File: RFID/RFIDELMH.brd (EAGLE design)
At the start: 21.6 x 39 mm, 3 parts, among them IC1 RFID_SENSOR, IC2 ARDUINO_PRO_MICRO

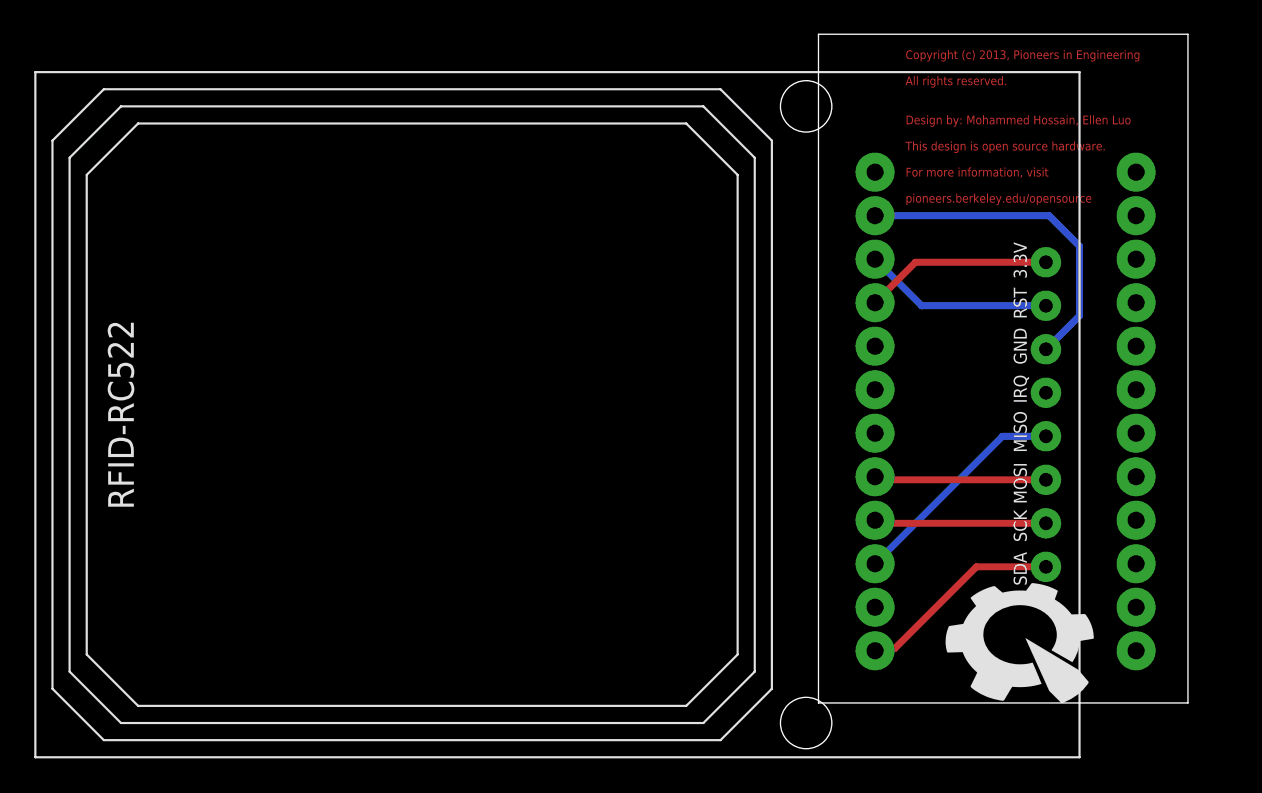
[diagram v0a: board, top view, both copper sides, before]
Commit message: Finish and flip RFID board
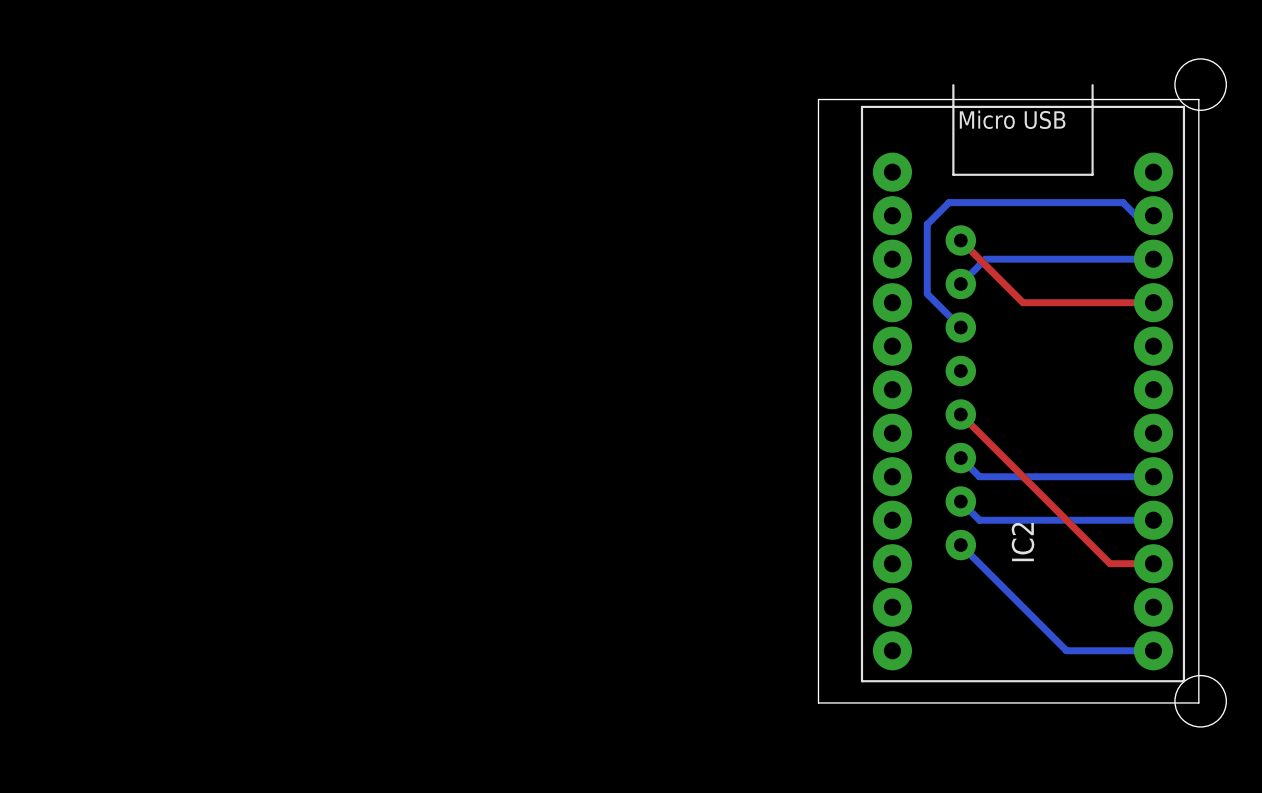
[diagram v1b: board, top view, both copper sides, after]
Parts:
- moved IC1 113.0 mm to (67.3, 38.1), flipped to the bottom
- moved IC2 17.8 mm to (2.54, 1.27), flipped to the top
- moved U$1 1.90 mm to (12.1, 5.71), flipped to the bottom
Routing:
- net SDA: track 12.0 -> 13.8 mm
- net MISO: track 13.1 -> 14.9 mm
- net VCC: track 11.0 -> 12.8 mm
- net SCK: track 10.1 -> 11.7 mm
- net MOSI: track 10.1 -> 11.7 mm
- net GND: track 19.5 -> 20.9 mm
- net RST: track 11.1 -> 11.8 mm
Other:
- board size 21.6 x 39 mm -> 22.2 x 35.2 mm
- board text added: "(c) Pioneers In Engineering Design by: Mohammed, Seiya, Averal, Ellen Catherine, Nick, Jillian, Lingfei, Ezra, Malcolm This design is open source hardware. For more information, visit: pioneers.berkeley.edu/opensource"
- board text removed: "Copyright (c) 2013, Pioneers in Engineering All rights reserved. Design by: Mohammed Hossain, Ellen Luo This design is open source hardware. For more information, visit pioneers.berkeley.edu/opensource"
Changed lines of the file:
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@@
 <layer number="27" name="tValues" color="7" fill="1" visible="yes" active="yes"/>
 <layer number="28" name="bValues" color="7" fill="1" visible="yes" active="yes"/>
-<layer number="29" name="tStop" color="7" fill="3" visible="no" active="yes"/>
-<layer number="30" name="bStop" color="7" fill="6" visible="no" active="yes"/>
-<layer number="31" name="tCream" color="7" fill="4" visible="no" active="yes"/>
-<layer number="32" name="bCream" color="7" fill="5" visible="no" active="yes"/>
-<layer number="33" name="tFinish" color="6" fill="3" visible="no" active="yes"/>
-<layer number="34" name="bFinish" color="6" fill="6" visible="no" active="yes"/>
-<layer number="35" name="tGlue" color="7" fill="4" visible="no" active="yes"/>
-<layer number="36" name="bGlue" color="7" fill="5" visible="no" active="yes"/>
-<layer number="37" name="tTest" color="7" fill="1" visible="no" active="yes"/>
-<layer number="38" name="bTest" color="7" fill="1" visible="no" active="yes"/>
+<layer number="29" name="tStop" color="7" fill="3" visible="yes" active="yes"/>
+<layer number="30" name="bStop" color="7" fill="6" visible="yes" active="yes"/>
+<layer number="31" name="tCream" color="7" fill="4" visible="yes" active="yes"/>
+<layer number="32" name="bCream" color="7" fill="5" visible="yes" active="yes"/>
+<layer number="33" name="tFinish" color="6" fill="3" visible="yes" active="yes"/>
+<layer number="34" name="bFinish" color="6" fill="6" visible="yes" active="yes"/>
+<layer number="35" name="tGlue" color="7" fill="4" visible="yes" active="yes"/>
+<layer number="36" name="bGlue" color="7" fill="5" visible="yes" active="yes"/>
+<layer number="37" name="tTest" color="7" fill="1" visible="yes" active="yes"/>
+<layer number="38" name="bTest" color="7" fill="1" visible="yes" active="yes"/>
 <layer number="39" name="tKeepout" color="4" fill="11" visible="yes" active="yes"/>
 <layer number="40" name="bKeepout" color="1" fill="11" visible="yes" active="yes"/>
@@
 <layer number="42" name="bRestrict" color="1" fill="10" visible="yes" active="yes"/>
 <layer number="43" name="vRestrict" color="2" fill="10" visible="yes" active="yes"/>
-<layer number="44" name="Drills" color="7" fill="1" visible="no" active="yes"/>
-<layer number="45" name="Holes" color="7" fill="1" visible="no" active="yes"/>
-<layer number="46" name="Milling" color="3" fill="1" visible="no" active="yes"/>
-<layer number="47" name="Measures" color="7" fill="1" visible="no" active="yes"/>
+<layer number="44" name="Drills" color="7" fill="1" visible="yes" active="yes"/>
+<layer number="45" name="Holes" color="7" fill="1" visible="yes" active="yes"/>
+<layer number="46" name="Milling" color="3" fill="1" visible="yes" active="yes"/>
+<layer number="47" name="Measures" color="7" fill="1" visible="yes" active="yes"/>
 <layer number="48" name="Document" color="7" fill="1" visible="yes" active="yes"/>
 <layer number="49" name="Reference" color="7" fill="1" visible="yes" active="yes"/>
@@
 <board>
 <plain>
-<wire x1="0" y1="0" x2="21.57" y2="0" width="0" layer="20"/>
-<wire x1="21.57" y1="0" x2="21.57" y2="39.04" width="0" layer="20"/>
-<wire x1="21.57" y1="39.04" x2="0" y2="39.04" width="0" layer="20"/>
-<wire x1="0" y1="39.04" x2="0" y2="0" width="0" layer="20"/>
-<text x="5.08" y="29.21" size="0.508" layer="1">Copyright (c) 2013, Pioneers in Engineering
-All rights reserved.
-Design by: Mohammed Hossain, Ellen Luo
+<wire x1="0" y1="0" x2="22.205" y2="0" width="0" layer="20"/>
+<wire x1="22.205" y1="0" x2="22.205" y2="35.23" width="0" layer="20"/>
+<wire x1="22.205" y1="35.23" x2="0" y2="35.23" width="0" layer="20"/>
+<wire x1="0" y1="35.23" x2="0" y2="0" width="0" layer="20"/>
+<text x="12.7" y="29.21" size="0.508" layer="23" font="vector" rot="R270">(c) Pioneers In Engineering
+Design by: Mohammed, Seiya, Averal, Ellen
+Catherine, Nick, Jillian, Lingfei, Ezra, Malcolm
 This design is open source hardware.
-For more information, visit
+For more information, visit:
 pioneers.berkeley.edu/opensource</text>
 </plain>
@@
 </autorouter>
 <elements>
-<element name="IC1" library="pie" package="RFID_SENSOR" value="RFID_SENSOR" x="-45.72" y="36.83" rot="R270"/>
-<element name="IC2" library="pie" package="ARDUINO_PRO_MICRO" value="ARDUINO_PRO_MICRO" x="20.32" y="1.27" rot="MR0"/>
-<element name="U$1" library="pie" package="PIE-LOGO-SMALL" value="" x="12.065" y="3.81"/>
+<element name="IC1" library="pie" package="RFID_SENSOR" value="RFID_SENSOR" x="67.31" y="38.1" rot="MR270"/>
+<element name="IC2" library="pie" package="ARDUINO_PRO_MICRO" value="ARDUINO_PRO_MICRO" x="2.54" y="1.27"/>
+<element name="U$1" library="pie" package="PIE-LOGO-SMALL" value="" x="12.065" y="5.715" rot="MR0"/>
 </elements>
 <signals>
@@
 <contactref element="IC2" pad="VCC"/>
 <contactref element="IC1" pad="3.3V"/>
-<wire x1="3.302" y1="23.368" x2="5.664" y2="25.73" width="0.4064" layer="1"/>
-<wire x1="5.664" y1="25.73" x2="13.28" y2="25.73" width="0.4064" layer="1"/>
+<wire x1="8.31" y1="27" x2="11.942" y2="23.368" width="0.4064" layer="1"/>
+<wire x1="11.942" y1="23.368" x2="19.558" y2="23.368" width="0.4064" layer="1"/>
 </signal>
 <signal name="RST">
 <contactref element="IC2" pad="RST"/>
 <contactref element="IC1" pad="RST"/>
-<wire x1="3.302" y1="25.908" x2="6.02" y2="23.19" width="0.4064" layer="16"/>
-<wire x1="6.02" y1="23.19" x2="13.28" y2="23.19" width="0.4064" layer="16"/>
+<wire x1="8.31" y1="24.46" x2="9.758" y2="25.908" width="0.4064" layer="16"/>
+<wire x1="9.758" y1="25.908" x2="19.558" y2="25.908" width="0.4064" layer="16"/>
 </signal>
 <signal name="GND">
 <contactref element="IC1" pad="GND"/>
 <contactref element="IC2" pad="GND@2"/>
-<wire x1="13.28" y1="20.65" x2="15.24" y2="22.61" width="0.4064" layer="16"/>
-<wire x1="15.24" y1="22.61" x2="15.24" y2="26.67" width="0.4064" layer="16"/>
-<wire x1="15.24" y1="26.67" x2="13.462" y2="28.448" width="0.4064" layer="16"/>
-<wire x1="13.462" y1="28.448" x2="3.302" y2="28.448" width="0.4064" layer="16"/>
+<wire x1="8.31" y1="21.92" x2="6.35" y2="23.88" width="0.4064" layer="16"/>
+<wire x1="6.35" y1="23.88" x2="6.35" y2="27.94" width="0.4064" layer="16"/>
+<wire x1="6.35" y1="27.94" x2="7.62" y2="29.21" width="0.4064" layer="16"/>
+<wire x1="7.62" y1="29.21" x2="17.78" y2="29.21" width="0.4064" layer="16"/>
+<wire x1="17.78" y1="29.21" x2="18.542" y2="28.448" width="0.4064" layer="16"/>
+<wire x1="18.542" y1="28.448" x2="19.558" y2="28.448" width="0.4064" layer="16"/>
 </signal>
 <signal name="SDA">
 <contactref element="IC2" pad="10"/>
 <contactref element="IC1" pad="SDA"/>
-<wire x1="13.28" y1="7.95" x2="9.22" y2="7.95" width="0.4064" layer="1"/>
-<wire x1="9.22" y1="7.95" x2="4.445" y2="3.175" width="0.4064" layer="1"/>
-<wire x1="4.445" y1="3.175" x2="3.302" y2="3.048" width="0.4064" layer="1"/>
+<wire x1="8.31" y1="9.22" x2="14.482" y2="3.048" width="0.4064" layer="16"/>
+<wire x1="14.482" y1="3.048" x2="19.558" y2="3.048" width="0.4064" layer="16"/>
 </signal>
 <signal name="MOSI">
 <contactref element="IC2" pad="A0"/>
 <contactref element="IC1" pad="MOSI"/>
-<wire x1="13.28" y1="13.03" x2="3.48" y2="13.03" width="0.4064" layer="1"/>
-<wire x1="3.48" y1="13.03" x2="3.302" y2="13.208" width="0.4064" layer="1"/>
+<wire x1="8.31" y1="14.3" x2="9.402" y2="13.208" width="0.4064" layer="16"/>
+<wire x1="9.402" y1="13.208" x2="19.558" y2="13.208" width="0.4064" layer="16"/>
 </signal>
 <signal name="MISO">
 <contactref element="IC2" pad="14"/>
 <contactref element="IC1" pad="MISO"/>
-<wire x1="13.28" y1="15.57" x2="10.744" y2="15.57" width="0.4064" layer="16"/>
-<wire x1="10.744" y1="15.57" x2="3.302" y2="8.128" width="0.4064" layer="16"/>
+<wire x1="8.31" y1="16.84" x2="17.022" y2="8.128" width="0.4064" layer="1"/>
+<wire x1="17.022" y1="8.128" x2="19.558" y2="8.128" width="0.4064" layer="1"/>
 </signal>
 <signal name="SCK">
 <contactref element="IC2" pad="15"/>
 <contactref element="IC1" pad="SCK"/>
-<wire x1="13.28" y1="10.49" x2="3.48" y2="10.49" width="0.4064" layer="1"/>
-<wire x1="3.48" y1="10.49" x2="3.302" y2="10.668" width="0.4064" layer="1"/>
+<wire x1="8.31" y1="11.76" x2="9.402" y2="10.668" width="0.4064" layer="16"/>
+<wire x1="9.402" y1="10.668" x2="19.558" y2="10.668" width="0.4064" layer="16"/>
 </signal>
 </signals>
